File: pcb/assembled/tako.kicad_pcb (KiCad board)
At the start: 4 copper layers, 230.7 x 97.8 mm, 146 parts, among them J1 MJ-4PP-9, J101 MJ-4PP-9, J102 OLED, J2 OLED, SW1 EC_SW, SW10 EC_SW, SW101 EC_SW, SW102 EC_SW, SW103 EC_SW, SW104 EC_SW, SW105 EC_SW, SW106 EC_SW, SW107 EC_SW, SW108 EC_SW, SW109 EC_SW, SW11 EC_SW, SW110 EC_SW, SW111 EC_SW, SW112 EC_SW, SW113 EC_SW, SW114 EC_SW, SW115 EC_SW, SW116 EC_SW, SW117 EC_SW, SW12 EC_SW, SW13 EC_SW, SW14 EC_SW, SW15 EC_SW, SW16 EC_SW, SW17 EC_SW, SW2 EC_SW, SW3 EC_SW, SW4 EC_SW, SW5 EC_SW, SW6 EC_SW, SW7 EC_SW, SW8 EC_SW, SW9 EC_SW, U1 STM32F401CBUx, U101 STM32F401CBUx, U102 XC6206PxxxMR, U103 OPA350, U104 74HC4051, U2 XC6206PxxxMR, U3 OPA350, U4 74HC4051, Y1 8 MHz, Y101 8 MHz

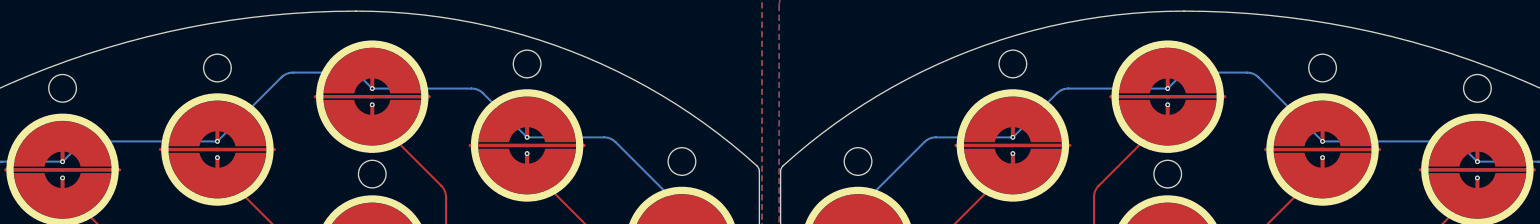
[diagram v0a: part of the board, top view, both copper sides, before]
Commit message: Align mounting holes to by in sync with diy version
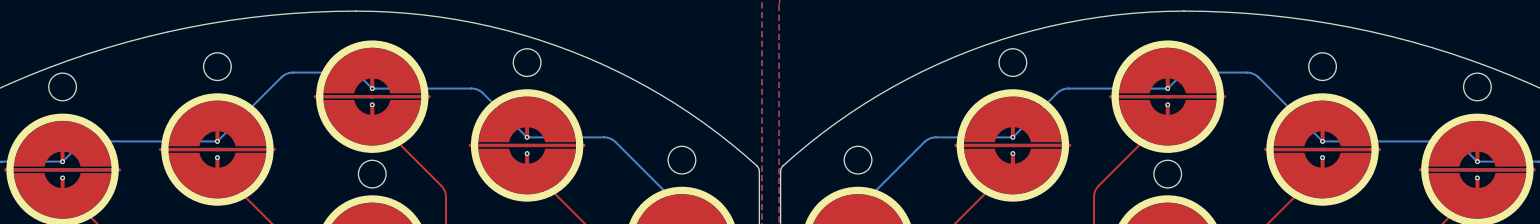
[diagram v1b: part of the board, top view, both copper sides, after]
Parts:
- moved H104 0.17 mm to (118.2, 56.6)
- moved H109 0.17 mm to (80.1, 57.1)
- moved H4 0.17 mm to (178.0, 56.6)
- moved H9 0.17 mm to (216.1, 57.1)
- moved H1 0.17 mm to (158.9, 68.6)
- moved H10 0.17 mm to (235.1, 59.6)
- moved H101 0.17 mm to (137.2, 68.6)
- moved H110 0.17 mm to (61.0, 59.6)
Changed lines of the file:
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@@
   )
   (footprint "local:MountingHole_3.4mm" (layer "F.Cu")
-    (at 216.055485 57.237644)
+    (at 216.055485 57.0682)
     (descr "Mounting Hole 2.2mm, no annular, M2")
     (tags "mounting hole 2.2mm no annular m2")
@@
   )
   (footprint "local:MountingHole_3.4mm" (layer "F.Cu")
-    (at 235.105483 59.737639)
+    (at 235.105483 59.568195)
     (descr "Mounting Hole 2.2mm, no annular, M2")
     (tags "mounting hole 2.2mm no annular m2")
@@
   )
   (footprint "local:MountingHole_3.4mm" (layer "F.Cu")
-    (at 177.95548 56.738145)
+    (at 177.95548 56.568701)
     (descr "Mounting Hole 2.2mm, no annular, M2")
     (tags "mounting hole 2.2mm no annular m2")
@@
   )
   (footprint "local:MountingHole_3.4mm" (layer "F.Cu")
-    (at 158.905476 68.738141)
+    (at 158.905476 68.568697)
     (descr "Mounting Hole 2.2mm, no annular, M2")
     (tags "mounting hole 2.2mm no annular m2")
@@
   )
   (footprint "local:MountingHole_3.4mm" (layer "B.Cu")
-    (at 61.04288 59.737639 180)
+    (at 61.04288 59.568195 180)
     (descr "Mounting Hole 2.2mm, no annular, M2")
     (tags "mounting hole 2.2mm no annular m2")
@@
   )
   (footprint "local:MountingHole_3.4mm" (layer "B.Cu")
-    (at 118.192883 56.738145 180)
+    (at 118.192883 56.568701 180)
     (descr "Mounting Hole 2.2mm, no annular, M2")
     (tags "mounting hole 2.2mm no annular m2")
@@
   )
   (footprint "local:MountingHole_3.4mm" (layer "B.Cu")
-    (at 80.092878 57.237644 180)
+    (at 80.092878 57.0682 180)
     (descr "Mounting Hole 2.2mm, no annular, M2")
     (tags "mounting hole 2.2mm no annular m2")
@@
   )
   (footprint "local:MountingHole_3.4mm" (layer "B.Cu")
-    (at 137.242887 68.738141 180)
+    (at 137.242887 68.568697 180)
     (descr "Mounting Hole 2.2mm, no annular, M2")
     (tags "mounting hole 2.2mm no annular m2")
